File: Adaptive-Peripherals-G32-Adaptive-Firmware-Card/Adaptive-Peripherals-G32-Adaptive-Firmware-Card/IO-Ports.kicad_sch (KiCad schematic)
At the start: 49 parts, among them J1 Conn_02x07_Odd_Even, J2 Conn_02x10_Odd_Even, Q1 PN2222A, Q2 2N3906, Q3 2N3906, Q4 PN2222A, Q5 PN2222A, Q6 2N3906, U1 LM339, U2 74LS374, U3 74HC244, U4 74HC244, U5 74HC244, U7 74HC00

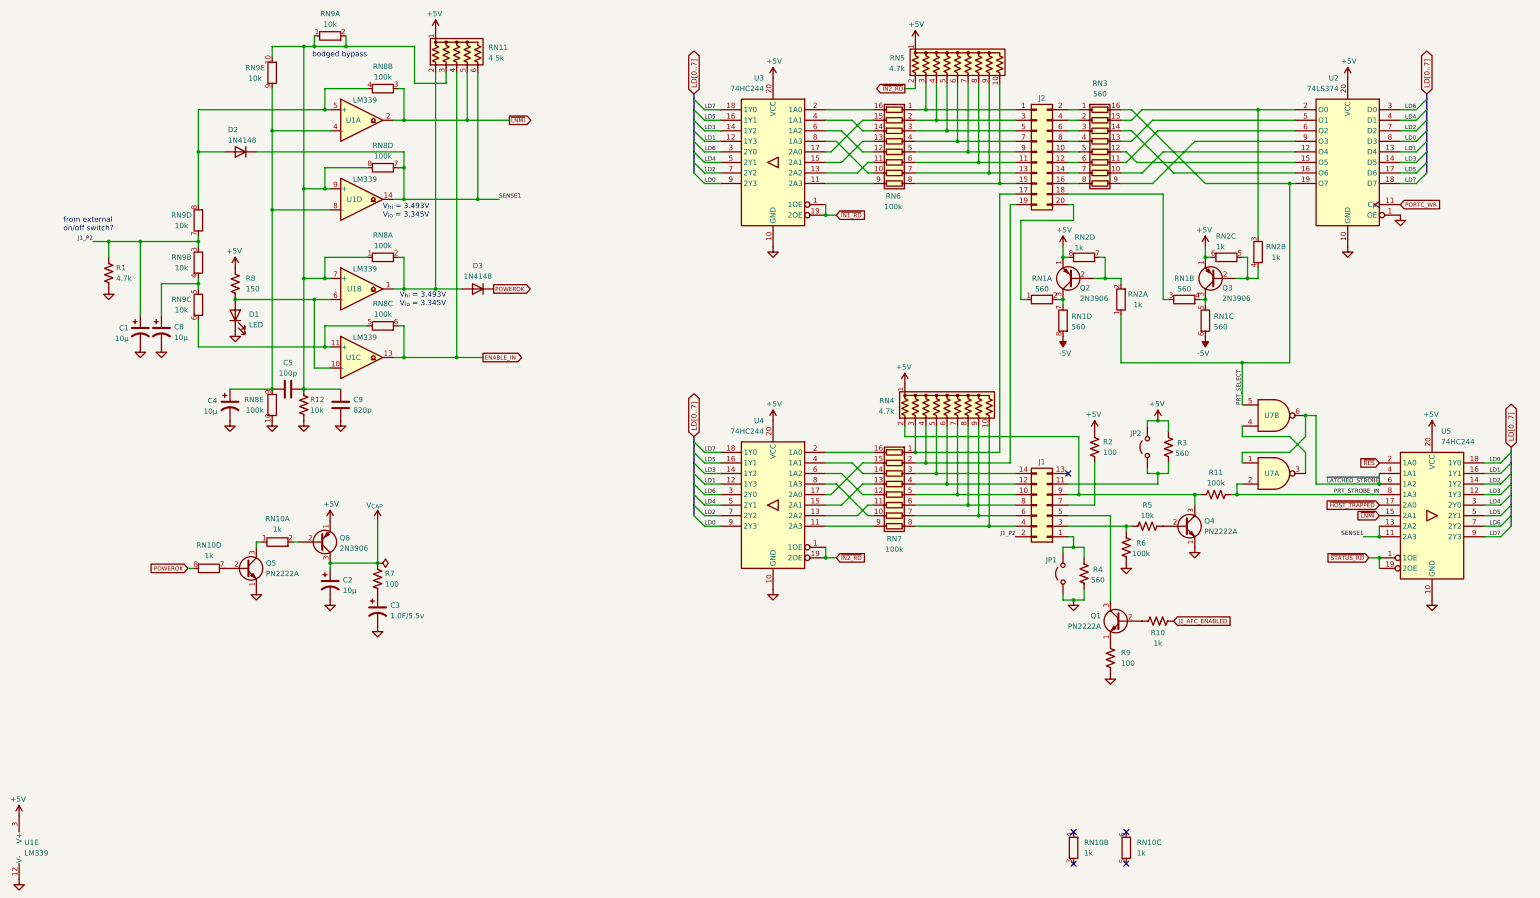
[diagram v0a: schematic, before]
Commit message: Add breakout box information for the Adaptive Peripherals card
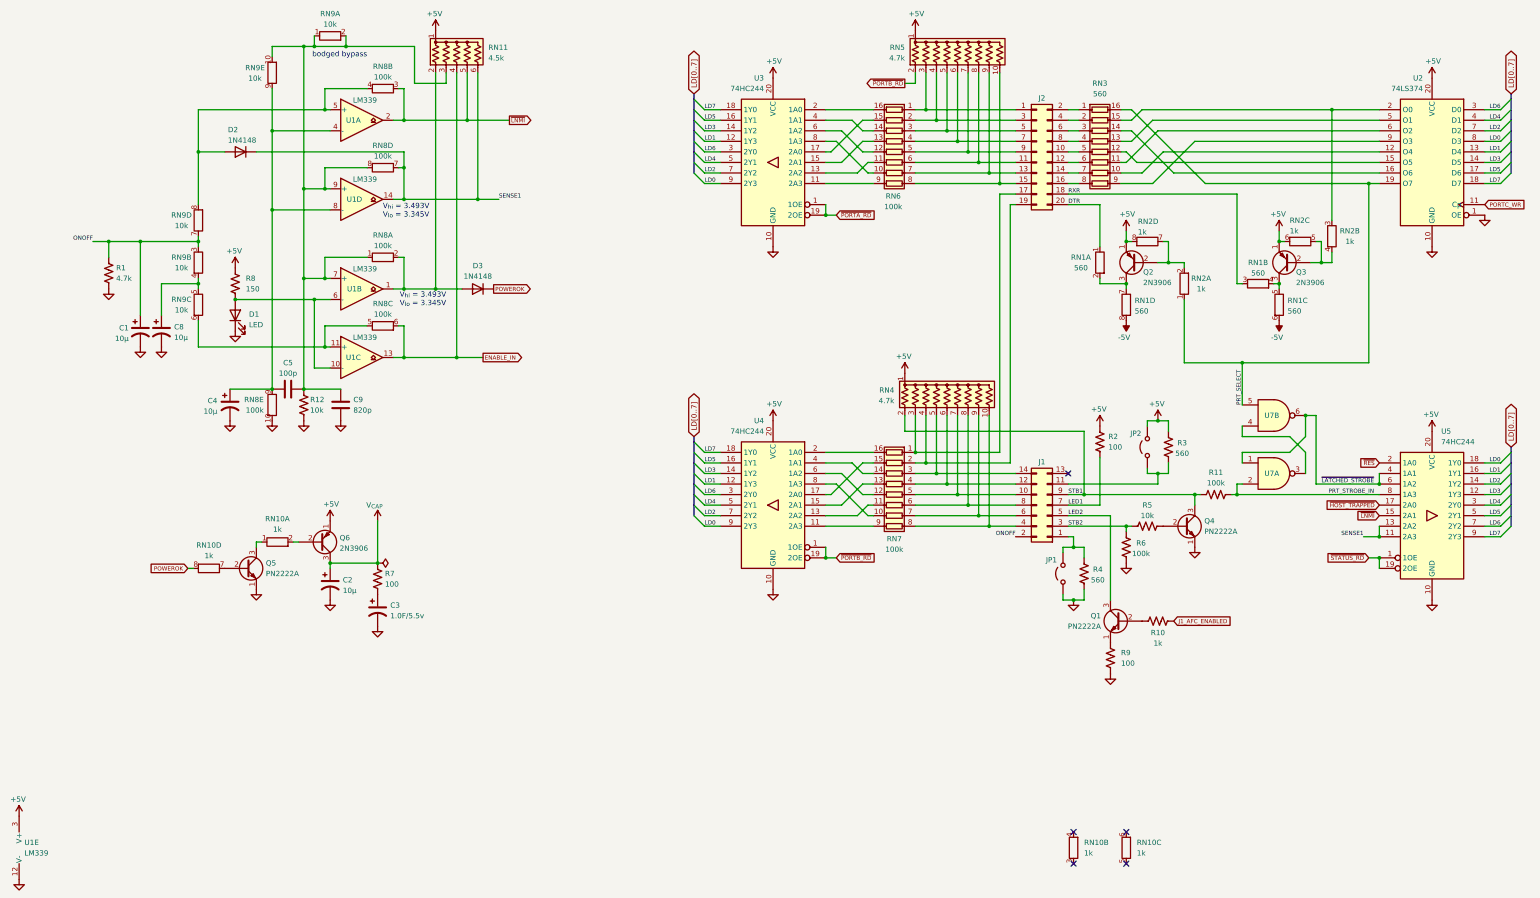
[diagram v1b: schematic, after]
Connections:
- net STB2: now reaches J1.3 (Pin_3), R5.2, R6.1
- net STB1: now reaches J1.9 (Pin_9), Q4.3 (C), R11.1, RN4.2 (R1)
- net LED2: now reaches J1.5 (Pin_5), Q1.3 (C)
- net LED1: now reaches J1.7 (Pin_7), R2.2
- net RXR: now reaches J2.18 (Pin_18), RN1.3 (R2.1)
- net DTR: now reaches J2.20 (Pin_20), RN1.1 (R1.1)
- net J1_P2 renamed ONOFF
- net ~{IN1_RD} renamed ~{PORTA_RD}
- net ~{IN2_RD} renamed ~{PORTB_RD}
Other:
- note removed: "from external on/off switch?"
- moved on the sheet: Q2, Q3, R2, RN1A, RN1B, RN1C, RN1D, RN2A, RN2B, RN2C, RN2D, RN4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
